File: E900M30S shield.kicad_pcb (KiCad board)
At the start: 2 copper layers, 55 x 40 mm, 5 parts, among them J1 Conn10, J2 Conn02, U1 E22-900M30S

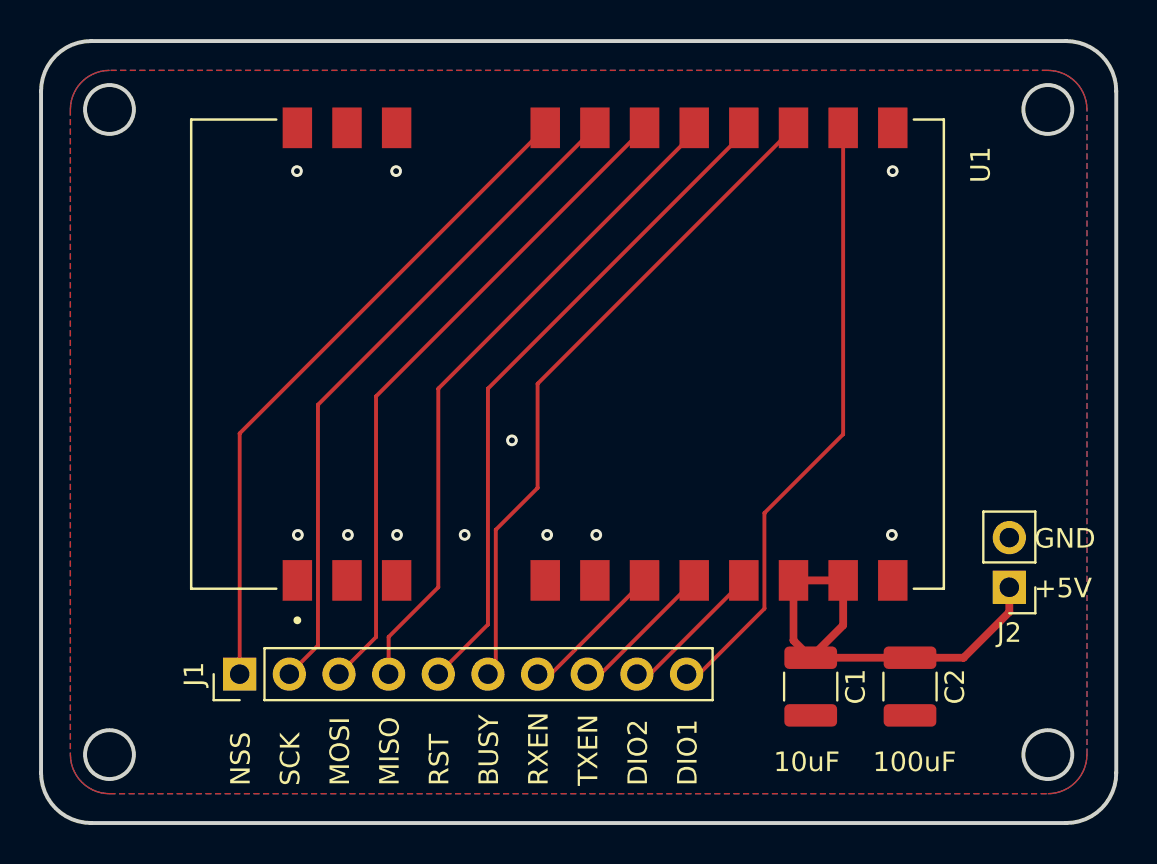
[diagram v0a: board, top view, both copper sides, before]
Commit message: Redesign to keep tracks away from under the module as per datasheet
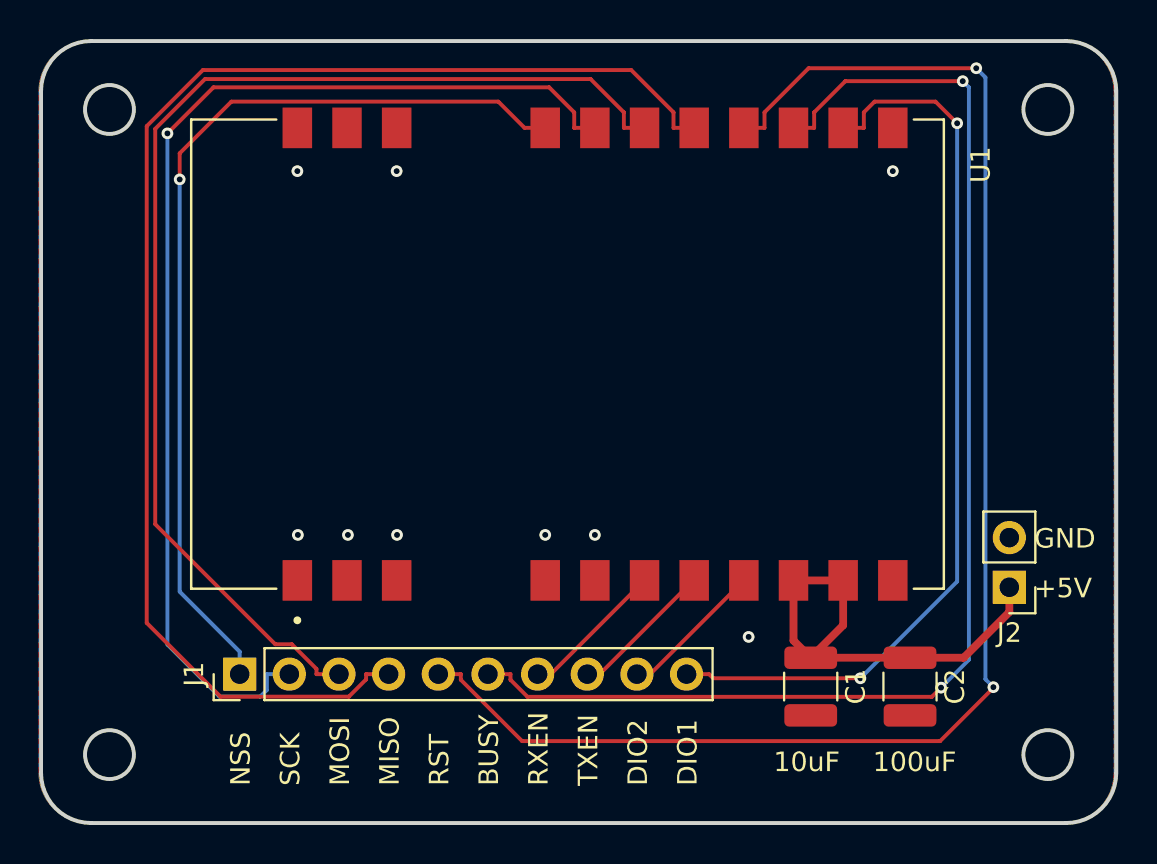
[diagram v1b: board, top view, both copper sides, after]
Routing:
- net RST: track 34.4 -> 76.8 mm, vias 0 -> 2
- net MISO: track 34.4 -> 70.9 mm
- net BUSY: track 34.9 -> 65.9 mm, vias 0 -> 2
- net MOSI: track 34.4 -> 60.5 mm
- net SCK: track 34.4 -> 58.6 mm, vias 0 -> 1
- net DIO1: track 31.6 -> 46.7 mm, vias 0 -> 2
- net NSS: track 34.4 -> 48.3 mm, vias 0 -> 1
- net GND: track 1.13 -> 0.00 mm, vias 11 -> 9

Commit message: Redesign to keep tracks off from under the module
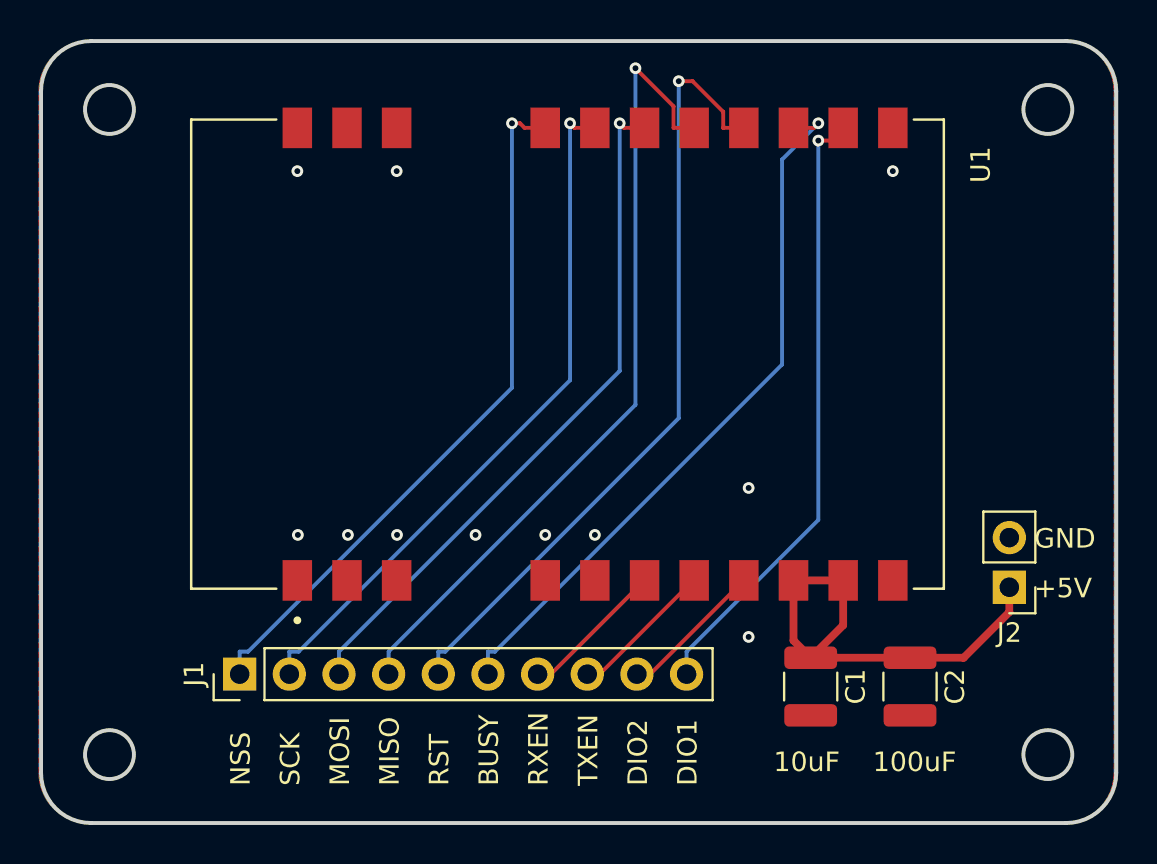
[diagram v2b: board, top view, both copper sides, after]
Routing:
- net RST: track 76.8 -> 40.4 mm, vias 2 -> 1
- net MISO: track 70.9 -> 41.1 mm, vias 0 -> 1
- net BUSY: track 65.9 -> 36.8 mm, vias 2 -> 1
- net MOSI: track 60.5 -> 35.5 mm, vias 0 -> 1
- net SCK: track 58.6 -> 35.8 mm
- net DIO1: track 46.7 -> 31.6 mm, vias 2 -> 1
- net NSS: track 48.3 -> 36.0 mm
- net GND: vias 9 -> 11
